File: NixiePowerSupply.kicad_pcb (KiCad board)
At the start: 2 copper layers, 57.2 x 40.6 mm, 32 parts, among them J1 BARREL_JACK, P1 CONN_01X03, P2 CONN_01X03, T1 IRF644, U1 MAX1771

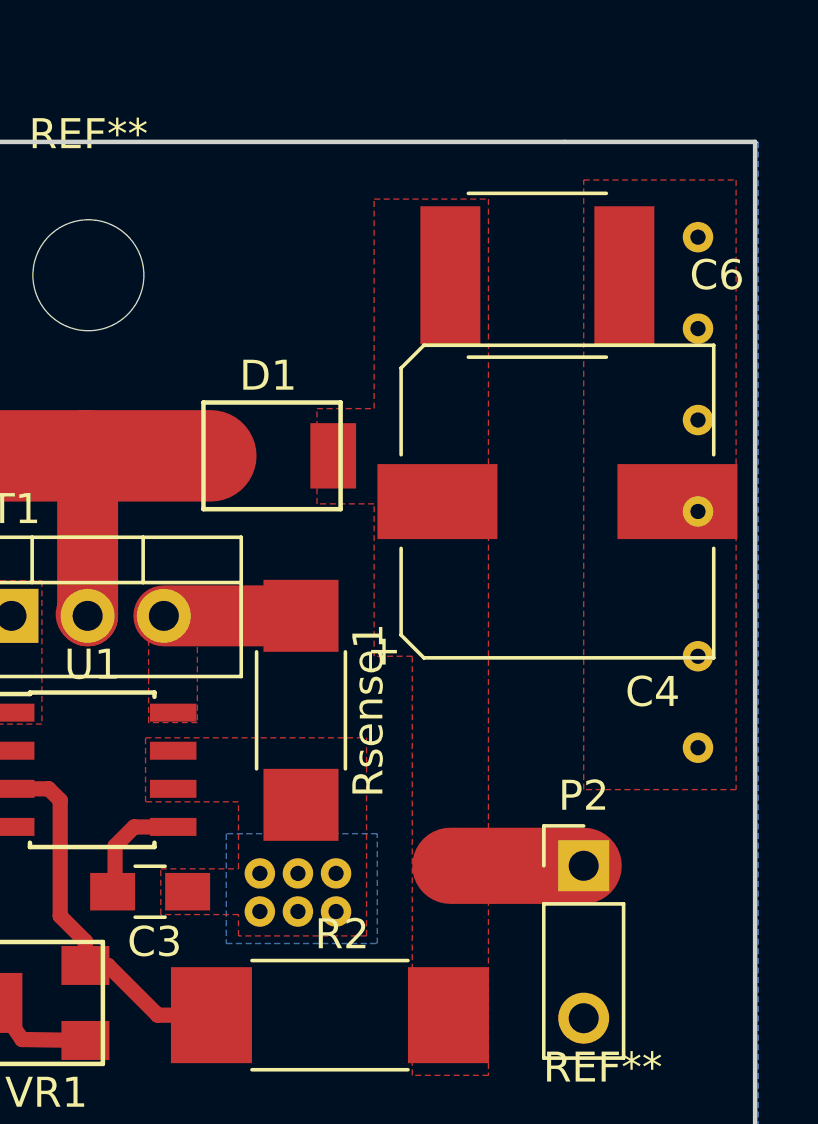
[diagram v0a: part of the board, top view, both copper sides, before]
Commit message: Fix via stitching
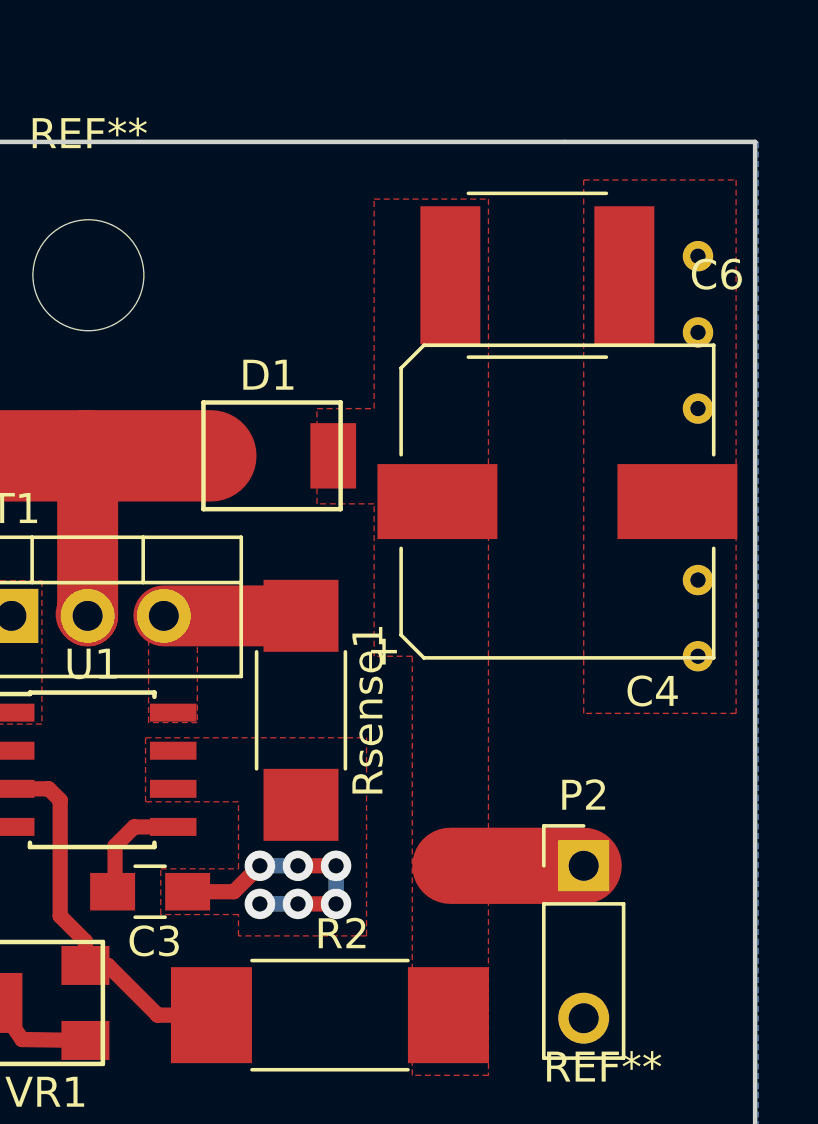
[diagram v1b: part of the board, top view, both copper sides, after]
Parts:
- removed the REF** at (167.6, 100.6)
- removed the REF** at (165.1, 99.3)
- removed the REF** at (166.4, 100.6)
- removed the REF** at (165.1, 100.6)
- removed the REF** at (167.6, 99.3)
- removed the REF** at (166.4, 99.3)
- removed the REF** at (179.7, 95.1)
- moved REF** 2.29 mm to (179.7, 89.5)
- moved REF** 0.63 mm to (179.7, 78.7)
- moved REF** 0.38 mm to (179.7, 83.8)
- moved REF** 0.13 mm to (179.7, 81.3)
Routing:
- net GND: track 13.7 -> 22.8 mm, vias 3 -> 9
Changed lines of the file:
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@@
-(kicad_pcb (version 4) (host pcbnew 4.0.6)
+(kicad_pcb (version 4) (host pcbnew 4.0.5)
   (general
-    (links 0)
-    (no_connects 1)
+    (links 40)
+    (no_connects 0)
     (area 121.357429 70.963399 184.712572 116.319)
     (thickness 1.6)
     (drawings 6)
-    (tracks 69)
+    (tracks 82)
     (zones 0)
-    (modules 32)
+    (modules 25)
     (nets 11)
   )
@@
   )
   (setup
-    (last_trace_width 0.25)
+    (last_trace_width 0.508)
     (user_trace_width 0.508)
     (user_trace_width 1.016)
@@
     (user_trace_width 3.048)
     (trace_clearance 0.2)
-    (zone_clearance 0.254)
+    (zone_clearance 0)
     (zone_45_only yes)
     (trace_min 0.2)
@@
     (add_net "Net-(Rsense1-Pad1)")
   )
-  (module nixie:Via (layer F.Cu)
-    (at 167.64 100.584)
-    (fp_text reference REF** (at 0.127 4.064) (layer F.SilkS) hide
-      (effects (font (size 1 1) (thickness 0.15)))
-    )
-    (fp_text value Via (at 0 -4.572) (layer F.Fab) hide
-      (effects (font (size 1 1) (thickness 0.15)))
-    )
-    (pad 1 thru_hole circle (at 0 0) (size 1.016 1.016) (drill 0.508) (layers *.Cu)
-      (net 1 GND) (zone_connect 2))
-  )
-  (module nixie:Via (layer F.Cu)
-    (at 166.37 100.584)
-    (fp_text reference REF** (at 0.127 4.064) (layer F.SilkS) hide
-      (effects (font (size 1 1) (thickness 0.15)))
-    )
-    (fp_text value Via (at 0 -4.572) (layer F.Fab) hide
-      (effects (font (size 1 1) (thickness 0.15)))
-    )
-    (pad 1 thru_hole circle (at 0 0) (size 1.016 1.016) (drill 0.508) (layers *.Cu)
-      (net 1 GND) (zone_connect 2))
-  )
-  (module nixie:Via (layer F.Cu)
-    (at 165.1 100.584)
-    (fp_text reference REF** (at 0.127 4.064) (layer F.SilkS) hide
-      (effects (font (size 1 1) (thickness 0.15)))
-    )
-    (fp_text value Via (at 0 -4.572) (layer F.Fab) hide
-      (effects (font (size 1 1) (thickness 0.15)))
-    )
-    (pad 1 thru_hole circle (at 0 0) (size 1.016 1.016) (drill 0.508) (layers *.Cu)
-      (net 1 GND) (zone_connect 2))
-  )
-  (module nixie:Via (layer F.Cu)
-    (at 167.64 99.314)
-    (fp_text reference REF** (at 0.127 4.064) (layer F.SilkS) hide
-      (effects (font (size 1 1) (thickness 0.15)))
-    )
-    (fp_text value Via (at 0 -4.572) (layer F.Fab) hide
-      (effects (font (size 1 1) (thickness 0.15)))
-    )
-    (pad 1 thru_hole circle (at 0 0) (size 1.016 1.016) (drill 0.508) (layers *.Cu)
-      (net 1 GND) (zone_connect 2))
-  )
-  (module nixie:Via (layer F.Cu)
-    (at 166.37 99.314)
-    (fp_text reference REF** (at 0.127 4.064) (layer F.SilkS) hide
-      (effects (font (size 1 1) (thickness 0.15)))
-    )
-    (fp_text value Via (at 0 -4.572) (layer F.Fab) hide
-      (effects (font (size 1 1) (thickness 0.15)))
-    )
-    (pad 1 thru_hole circle (at 0 0) (size 1.016 1.016) (drill 0.508) (layers *.Cu)
-      (net 1 GND) (zone_connect 2))
-  )
   (module Mounting_Holes:MountingHole_3.7mm (layer F.Cu)
     (at 159.385 79.375)
@@
   )
   (module nixie:Via (layer F.Cu)
-    (at 179.705 95.123)
+    (at 179.705 89.535)
     (fp_text reference REF** (at 0.127 4.064) (layer F.SilkS) hide
       (effects (font (size 1 1) (thickness 0.15)))
@@
   )
   (module nixie:Via (layer F.Cu)
-    (at 179.705 87.249)
+    (at 179.705 83.82)
     (fp_text reference REF** (at 0.127 4.064) (layer F.SilkS) hide
       (effects (font (size 1 1) (thickness 0.15)))
@@
   )
   (module nixie:Via (layer F.Cu)
-    (at 179.705 84.201)
+    (at 179.705 81.28)
     (fp_text reference REF** (at 0.127 4.064) (layer F.SilkS) hide
       (effects (font (size 1 1) (thickness 0.15)))
@@
   )
   (module nixie:Via (layer F.Cu)
-    (at 179.705 81.153)
-    (fp_text reference REF** (at 0.127 4.064) (layer F.SilkS) hide
-      (effects (font (size 1 1) (thickness 0.15)))
-    )
-    (fp_text value Via (at 0 -4.572) (layer F.Fab) hide
-      (effects (font (size 1 1) (thickness 0.15)))
-    )
-    (pad 1 thru_hole circle (at 0 0) (size 1.016 1.016) (drill 0.508) (layers *.Cu *.Mask)
-      (net 1 GND) (zone_connect 2))
-  )
-  (module nixie:Via (layer F.Cu)
-    (at 179.705 78.105)
+    (at 179.705 78.74)
     (fp_text reference REF** (at 0.127 4.064) (layer F.SilkS) hide
       (effects (font (size 1 1) (thickness 0.15)))
@@
     )
   )
-  (module nixie:Via (layer F.Cu)
-    (at 165.1 99.314)
-    (fp_text reference REF** (at 0.127 4.064) (layer F.SilkS) hide
-      (effects (font (size 1 1) (thickness 0.15)))
-    )
-    (fp_text value Via (at 0 -4.572) (layer F.Fab) hide
-      (effects (font (size 1 1) (thickness 0.15)))
-    )
-    (pad 1 thru_hole circle (at 0 0) (size 1.016 1.016) (drill 0.508) (layers *.Cu)
-      (net 1 GND) (zone_connect 2))
-  )
   (gr_line (start 124.46 113.03) (end 124.46 115.57) (layer Edge.Cuts) (width 0.15))
   (gr_line (start 181.61 74.93) (end 181.61 115.57) (layer Edge.Cuts) (width 0.15))
@@
   (gr_line (start 175.26 74.93) (end 124.46 74.93) (angle 90) (layer Edge.Cuts) (width 0.15))
   (gr_line (start 124.46 74.93) (end 124.46 113.03) (angle 90) (layer Edge.Cuts) (width 0.15))
+  (segment (start 166.37 100.33) (end 165.1 100.33) (width 0.508) (layer B.Cu) (net 1))
+  (via (at 165.1 100.33) (size 1.016) (drill 0.508) (layers F.Cu B.Cu) (net 1))
+  (segment (start 167.64 100.33) (end 166.37 100.33) (width 0.508) (layer F.Cu) (net 1))
+  (via (at 166.37 100.33) (size 1.016) (drill 0.508) (layers F.Cu B.Cu) (net 1))
+  (segment (start 167.64 99.06) (end 167.64 100.33) (width 0.508) (layer B.Cu) (net 1))
+  (via (at 167.64 100.33) (size 1.016) (drill 0.508) (layers F.Cu B.Cu) (net 1))
+  (segment (start 166.37 99.06) (end 167.64 99.06) (width 0.508) (layer F.Cu) (net 1))
+  (via (at 167.64 99.06) (size 1.016) (drill 0.508) (layers F.Cu B.Cu) (net 1))
+  (segment (start 165.1 99.06) (end 166.37 99.06) (width 0.508) (layer B.Cu) (net 1))
+  (via (at 166.37 99.06) (size 1.016) (drill 0.508) (layers F.Cu B.Cu) (net 1))
+  (segment (start 164.2364 99.9236) (end 165.1 99.06) (width 0.508) (layer F.Cu) (net 1))
+  (via (at 165.1 99.06) (size 1.016) (drill 0.508) (layers F.Cu B.Cu) (net 1))
+  (segment (start 162.6924 99.9236) (end 164.2364 99.9236) (width 0.508) (layer F.Cu) (net 1))
   (segment (start 133.6548 98.2122) (end 133.6548 101.7524) (width 1.016) (layer F.Cu) (net 1) (status 10))
   (via (at 133.604 101.8032) (size 2.032) (drill 1.016) (layers F.Cu B.Cu) (net 1))
@@
     (polygon
       (pts
-        (xy 175.895 76.2) (xy 180.975 76.2) (xy 180.975 96.52) (xy 175.895 96.52)
+        (xy 175.895 76.2) (xy 180.975 76.2) (xy 180.975 93.98) (xy 175.895 93.98)
       )
     )
@@
       )
     )
-  )
-  (zone (net 1) (net_name GND) (layer B.Cu) (hatch edge 0.508)
-    (priority 1)
-    (connect_pads yes (clearance 0.508))
-    (min_thickness 0.254)
-    (fill yes (arc_segments 16) (thermal_gap 0.508) (thermal_bridge_width 0.508) (smoothing chamfer) (radius 0.254))
-    (polygon
-      (pts
-        (xy 169.0116 97.9932) (xy 163.9824 97.9932) (xy 163.9824 101.6508) (xy 169.0116 101.6508)
-      )
-    )

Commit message: Trying to make a new board
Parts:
- removed C1: 100uF, 35V, Capacitors_Tantalum_SMD:CP_Tantalum_Case-X_EIA-7343-43_Hand
- removed C2, C3: 100n, Capacitors_SMD:C_0805_HandSoldering
- removed C4: 10uF,250V, Capacitors_SMD:CP_Elec_10x10
- removed C5: 10uF,25V, Capacitors_Tantalum_SMD:CP_Tantalum_Case-X_EIA-7343-43_Hand
- removed C6: 100nF, 250V, nixie:Panasonic_ECWU_Size_B
- removed D1: ES2F, nixie:ES2F
- removed J1: BARREL_JACK, Connectors:BARREL_JACK
- removed L1: 100uH, nixie:L-B82479A1
- removed P1: CONN_01X03, Pin_Headers:Pin_Header_Straight_1x03_Pitch2.54mm
- removed P2: CONN_01X03, nixie:Pin_Header_Straight_1x03_Pitch2.54mm_No_Center
- removed R1: 10K, Resistors_SMD:R_0805_HandSoldering
- removed R2: 1M5, Resistors_SMD:R_2512_HandSoldering
- removed REF** (x3): MountingHole_3.7mm, Mounting_Holes:MountingHole_3.7mm
- removed REF** (x5): Via, nixie:Via
- removed Rsense1: 50m, Resistors_SMD:R_2010_HandSoldering
- removed T1: IRF644, TO_SOT_Packages_THT:TO-220_Vertical
- removed U1: MAX1771, Housings_SOIC:SOIC-8_3.9x4.9mm_Pitch1.27mm
- removed VR1: 5K, nixie:Trimpot_Bourns_3214W
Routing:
- net Net-(C1-Pad1): track 49.7 -> 0.00 mm
- net Net-(P1-Pad2): track 33.6 -> 0.00 mm
- net GND: track 22.8 -> 0.00 mm, vias 9 -> 0
- net Net-(D1-Pad2): track 21.2 -> 0.00 mm
- net Net-(R2-Pad2): track 12.5 -> 0.00 mm
- net Net-(R1-Pad1): track 6.44 -> 0.00 mm
- net Net-(Rsense1-Pad1): track 4.57 -> 0.00 mm
- net Net-(C4-Pad1): track 4.46 -> 0.00 mm
- net Net-(C3-Pad1): track 3.76 -> 0.00 mm
- removed copper zone on B.Cu, net GND
- removed copper zone on F.Cu, net GND
- removed copper zone on F.Cu, net Net-(C4-Pad1)
- removed copper zone on F.Cu, net Net-(Rsense1-Pad1)
- removed copper zone on F.Cu, net Net-(T1-Pad1)
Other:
- board outline removed
- net class Gate drive removed
- net class High current removed
- rule pad_to_mask_clearance: 0.2 -> 0

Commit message: Footprints place; partially routed
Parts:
- added C1: 100uF, 35V, Capacitors_Tantalum_SMD:CP_Tantalum_Case-X_EIA-7343-43_Hand, F.Cu at (52.7, 45.1)
- added C2: 100n, Capacitors_SMD:C_0805_HandSoldering, F.Cu at (66.7, 43.2)
- added C3: 100n, Capacitors_SMD:C_0805_HandSoldering, F.Cu at (74.9, 47.0)
- added C4: 10uF,250V, Capacitors_SMD:CP_Elec_10x10, F.Cu at (84.5, 31.8)
- added C5: 10uF,25V, Capacitors_Tantalum_SMD:CP_Tantalum_Case-X_EIA-7343-43_Hand, F.Cu at (62.2, 47.0)
- added C6: 100nF, 250V, nixie:Panasonic_ECWU_Size_B, F.Cu at (88.9, 40.6)
- added D1: ES2F, nixie:ES2F, F.Cu at (74.9, 30.5)
- added J1: BARREL_JACK, Connectors:BARREL_JACK, F.Cu at (54.9, 55.9)
- added L1: 100uH, nixie:L-B82479A1, F.Cu at (55.9, 33.7)
- added P1: CONN_01X03, Pin_Headers:Pin_Header_Straight_1x03_Pitch2.54mm, F.Cu at (60.3, 55.9)
- added P2: CONN_01X02, nixie:Pin_Header_Straight_1x03_Pitch2.54mm_No_Center, F.Cu at (92.1, 47.0)
- added R1: 10K, Resistors_SMD:R_0805_HandSoldering, F.Cu at (71.8, 52.1)
- added R2: 1M5, Resistors_SMD:R_2512_HandSoldering, F.Cu at (85.7, 50.2)
- added Rsense1: 50m, Resistors_SMD:R_2010_HandSoldering, F.Cu at (79.4, 43.8)
- added T1: IRF644, TO_SOT_Packages_THT:TO-220_Vertical, F.Cu at (69.2, 36.2)
- added U1: MAX1771, Housings_SOIC:SOIC-8_3.9x4.9mm_Pitch1.27mm, F.Cu at (71.8, 42.5)
- added VR1: 5K, nixie:Trimpot_Bourns_3214W, F.Cu at (79.4, 52.7)
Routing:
- net Net-(C1-Pad1): track 0.00 -> 25.3 mm
- net Net-(D1-Pad2): track 0.00 -> 17.6 mm
- net GND: track 0.00 -> 14.1 mm, vias 0 -> 8
- added copper zone on B.Cu, net GND
- added copper zone on F.Cu, net GND
- added copper zone on F.Cu, net Net-(C4-Pad1)
- added copper zone on F.Cu, net Net-(Rsense1-Pad1)
- added copper zone on F.Cu, net Net-(T1-Pad1)
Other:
- board outline added: 50.8 x 38.1 mm
